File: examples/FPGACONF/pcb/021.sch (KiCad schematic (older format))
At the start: 25 parts, among them CN401 JST_SM04B-SRSS-TB, CN402 JST_SM04B-SRSS-TB, CN403 JST_SM04B-SRSS-TB, CN404 ZX62D-B-5PA8(30), U401 LP5907MFX-3.3/NOPB

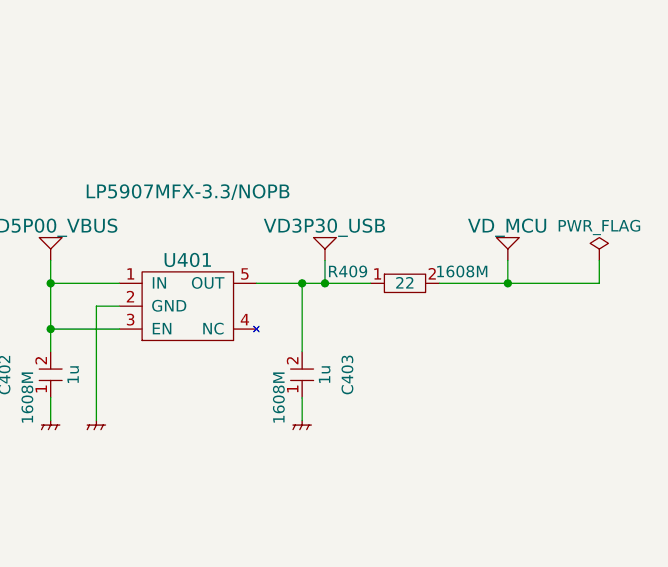
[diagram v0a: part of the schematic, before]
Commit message: 021.sch  R409 was chagned 0 ohm
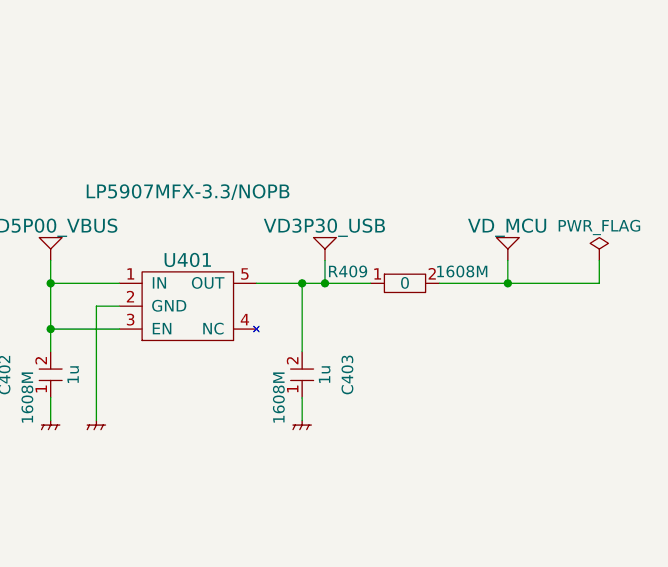
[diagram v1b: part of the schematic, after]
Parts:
- R409: value 22 -> 0
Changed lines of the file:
@@
 P 13200 2400
 F 0 "R409" H 13100 2450 50  0000 C CNN
-F 1 "22" H 13350 2400 50  0000 C CNN
+F 1 "0" H 13350 2400 50  0000 C CNN
 F 2 "zhtlab_SMD_standard:RCL_1608m" H 13000 2200 63  0001 C CNN
 F 3 "" H 13200 2550 79  0001 C CNN
